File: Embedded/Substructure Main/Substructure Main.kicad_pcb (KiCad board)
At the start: 2 copper layers, 47 parts, among them J1 MicroSD, J2 C Pins, U1 G0 FFC, U2 G1 FFC, U3 S FFC, U4 USB2513B_Bi, U5 MCP7940N-xMNY, U6 INA220AIDGSR, U8 F FFC, Y1 24MHz 18pF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

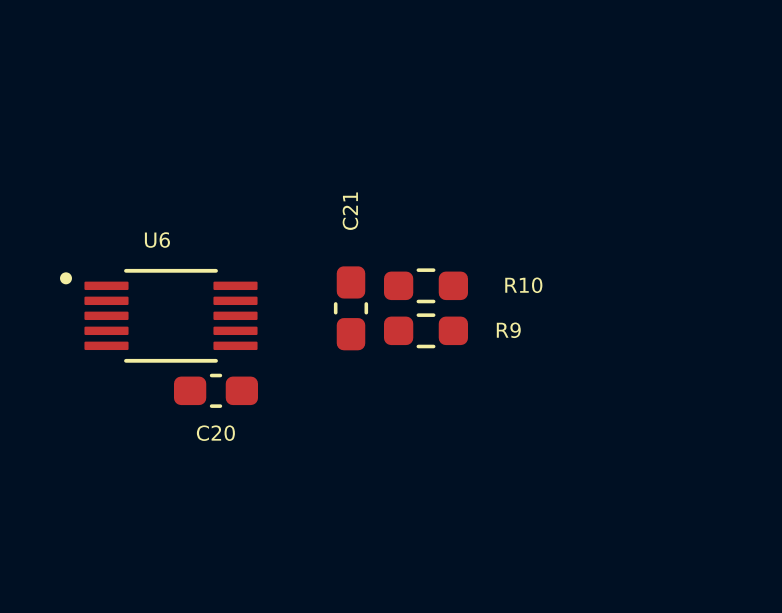
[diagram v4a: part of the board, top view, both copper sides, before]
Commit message: Added Shunt Resistor Footprint to PCB
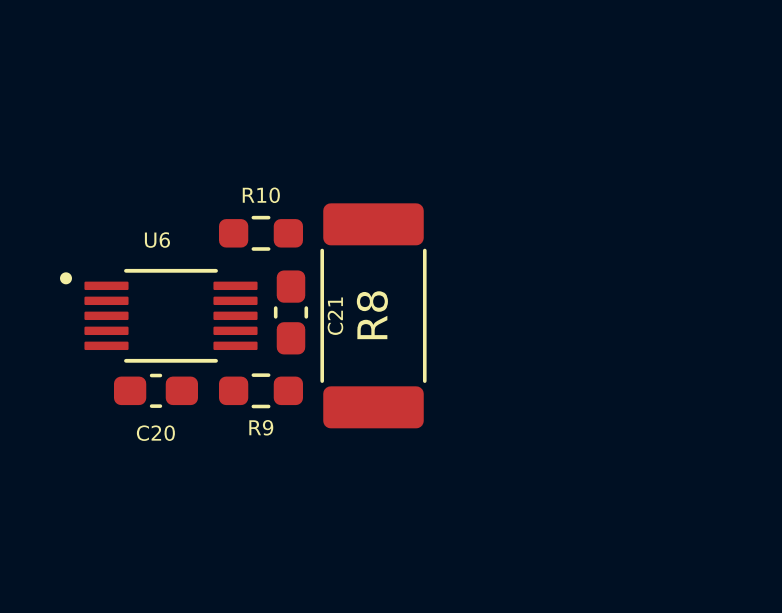
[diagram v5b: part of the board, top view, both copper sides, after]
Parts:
- added R8: Shunt, Resistor_SMD:R_2512_6332Metric_Pad1.40x3.35mm_HandSolder, F.Cu at (34.8, 184.5)
- moved R9 5.85 mm to (31.0, 187.0)
- moved R10 5.77 mm to (31.0, 181.8)
- moved C21 2.00 mm to (32.0, 184.4)
- moved C20 2.00 mm to (27.5, 187.0)
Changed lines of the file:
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@@
 	(footprint "Capacitor_SMD:C_0603_1608Metric_Pad1.08x0.95mm_HandSolder"
 		(layer "F.Cu")
-		(at 29.5 187 180)
+		(at 27.5 187 180)
 		(descr "Capacitor SMD 0603 (1608 Metric), square (rectangular) end terminal, IPC_7351 nominal with elongated pad for handsoldering. (Body size source: IPC-SM-782 page 76, https://www.pcb-3d.com/wordpress/wp-content/uploads/ipc-sm-782a_amendment_1_and_2.pdf), generated with kicad-footprint-generator")
 		(tags "capacitor handsolder")
@@
 	(footprint "Resistor_SMD:R_0603_1608Metric_Pad0.98x0.95mm_HandSolder"
 		(layer "F.Cu")
-		(at 36.5 183.5 180)
+		(at 31 181.75 180)
 		(descr "Resistor SMD 0603 (1608 Metric), square (rectangular) end terminal, IPC_7351 nominal with elongated pad for handsoldering. (Body size source: IPC-SM-782 page 72, https://www.pcb-3d.com/wordpress/wp-content/uploads/ipc-sm-782a_amendment_1_and_2.pdf), generated with kicad-footprint-generator")
 		(tags "resistor handsolder")
 		(property "Reference" "R10"
-			(at -3.25 0 0)
+			(at 0 1.25 0)
 			(layer "F.SilkS")
 			(effects
@@
 		)
 	)
+	(footprint "Resistor_SMD:R_2512_6332Metric_Pad1.40x3.35mm_HandSolder"
+		(layer "F.Cu")
+		(at 34.75 184.5 90)
+		(descr "Resistor SMD 2512 (6332 Metric), square (rectangular) end terminal, IPC_7351 nominal with elongated pad for handsoldering. (Body size source: IPC-SM-782 page 72, https://www.pcb-3d.com/wordpress/wp-content/uploads/ipc-sm-782a_amendment_1_and_2.pdf), generated with kicad-footprint-generator")
+		(tags "resistor handsolder")
+		(property "Reference" "R8"
+			(at 0 0 90)
+			(layer "F.SilkS")
+			(effects
+				(font
+					(size 1 1)
+					(thickness 0.15)
+				)
+			)
+		)
+		(property "Value" "Shunt"
+			(at 0 2.62 90)
+			(layer "F.Fab")
+			(hide yes)
+			(effects
+				(font
+					(size 1 1)
+					(thickness 0.15)
+				)
+			)
+		)
+		(property "Footprint" "Resistor_SMD:R_2512_6332Metric_Pad1.40x3.35mm_HandSolder"
+			(at 0 0 90)
+			(unlocked yes)
+			(layer "F.Fab")
+			(hide yes)
+			(effects
+				(font
+					(size 1.27 1.27)
+					(thickness 0.15)
+				)
+			)
+		)
+		(property "Datasheet" ""
+			(at 0 0 90)
+			(unlocked yes)
+			(layer "F.Fab")
+			(hide yes)
+			(effects
+				(font
+					(size 1.27 1.27)
+					(thickness 0.15)
+				)
+			)
+		)
+		(property "Description" "Resistor"
+			(at 0 0 90)
+			(unlocked yes)
+			(layer "F.Fab")
+			(hide yes)
+			(effects
+				(font
+					(size 1.27 1.27)
+					(thickness 0.15)
+				)
+			)
+		)
+		(property ki_fp_filters "R_*")
+		(sheetname "Root")
+		(sheetfile "Substructure Main.kicad_sch")
+		(attr smd)
+		(fp_line
+			(start -2.177064 -1.71)
+			(end 2.177064 -1.71)
+			(stroke
+				(width 0.12)
+				(type solid)
+			)
+			(layer "F.SilkS")
+		)
+		(fp_line
+			(start -2.177064 1.71)
+			(end 2.177064 1.71)
+			(stroke
+				(width 0.12)
+				(type solid)
+			)
+			(layer "F.SilkS")
+		)
+		(fp_line
+			(start 4 -1.92)
+			(end 4 1.92)
+			(stroke
+				(width 0.05)
+				(type solid)
+			)
+			(layer "F.CrtYd")
+		)
+		(fp_line
+			(start -4 -1.92)
+			(end 4 -1.92)
+			(stroke
+				(width 0.05)
+				(type solid)
+			)
+			(layer "F.CrtYd")
+		)
+		(fp_line
+			(start 4 1.92)
+			(end -4 1.92)
+			(stroke
+				(width 0.05)
+				(type solid)
+			)
+			(layer "F.CrtYd")
+		)
+		(fp_line
+			(start -4 1.92)
+			(end -4 -1.92)
+			(stroke
+				(width 0.05)
+				(type solid)
+			)
+			(layer "F.CrtYd")
+		)
+		(fp_line
+			(start 3.15 -1.6)
+			(end 3.15 1.6)
+			(stroke
+				(width 0.1)
+				(type solid)
+			)
+			(layer "F.Fab")
+		)
+		(fp_line
+			(start -3.15 -1.6)
+			(end 3.15 -1.6)
+			(stroke
+				(width 0.1)
+				(type solid)
+			)
+			(layer "F.Fab")
+		)
+		(fp_line
+			(start 3.15 1.6)
+			(end -3.15 1.6)
+			(stroke
+				(width 0.1)
+				(type solid)
+			)
+			(layer "F.Fab")
+		)
+		(fp_line
+			(start -3.15 1.6)
+			(end -3.15 -1.6)
+			(stroke
+				(width 0.1)
+				(type solid)
+			)
+			(layer "F.Fab")
+		)
+		(fp_text user "${REFERENCE}"
+			(at 0 0 90)
+			(layer "F.Fab")
+			(effects
+				(font
+					(size 1 1)
+					(thickness 0.15)
+				)
+			)
+		)
+		(pad "1" smd roundrect
+			(at -3.05 0 90)
+			(size 1.4 3.35)
+			(layers "F.Cu" "F.Paste" "F.Mask")
+			(roundrect_rratio 0.178571)
+			(net 13 "+5VP")
+			(pintype "passive")
+		)
+		(pad "2" smd roundrect
+			(at 3.05 0 90)
+			(size 1.4 3.35)
+			(layers "F.Cu" "F.Paste" "F.Mask")
+			(roundrect_rratio 0.178571)
+			(net 51 "+5V")
+			(pintype "passive")
+		)
+		(model "${KICAD8_3DMODEL_DIR}/Resistor_SMD.3dshapes/R_2512_6332Metric.wrl"
+			(offset
+				(xyz 0 0 0)
+			)
+			(scale
+				(xyz 1 1 1)
+			)
+			(rotate
+				(xyz 0 0 0)
+			)
+		)
+	)
 	(footprint "Capacitor_SMD:C_0402_1005Metric_Pad0.74x0.62mm_HandSolder"
 		(layer "F.Cu")
@@
 	(footprint "Capacitor_SMD:C_0603_1608Metric_Pad1.08x0.95mm_HandSolder"
 		(layer "F.Cu")
-		(at 34 184.25 90)
+		(at 32 184.3875 90)
 		(descr "Capacitor SMD 0603 (1608 Metric), square (rectangular) end terminal, IPC_7351 nominal with elongated pad for handsoldering. (Body size source: IPC-SM-782 page 76, https://www.pcb-3d.com/wordpress/wp-content/uploads/ipc-sm-782a_amendment_1_and_2.pdf), generated with kicad-footprint-generator")
 		(tags "capacitor handsolder")
 		(property "Reference" "C21"
-			(at 3.25 0 90)
+			(at -0.1125 1.5 90)
 			(layer "F.SilkS")
 			(effects
@@
 	(footprint "Resistor_SMD:R_0603_1608Metric_Pad0.98x0.95mm_HandSolder"
 		(layer "F.Cu")
-		(at 36.5 185 180)
+		(at 31 187 180)
 		(descr "Resistor SMD 0603 (1608 Metric), square (rectangular) end terminal, IPC_7351 nominal with elongated pad for handsoldering. (Body size source: IPC-SM-782 page 72, https://www.pcb-3d.com/wordpress/wp-content/uploads/ipc-sm-782a_amendment_1_and_2.pdf), generated with kicad-footprint-generator")
 		(tags "resistor handsolder")
 		(property "Reference" "R9"
-			(at -2.75 0 0)
+			(at 0 -1.25 0)
 			(layer "F.SilkS")
 			(effects

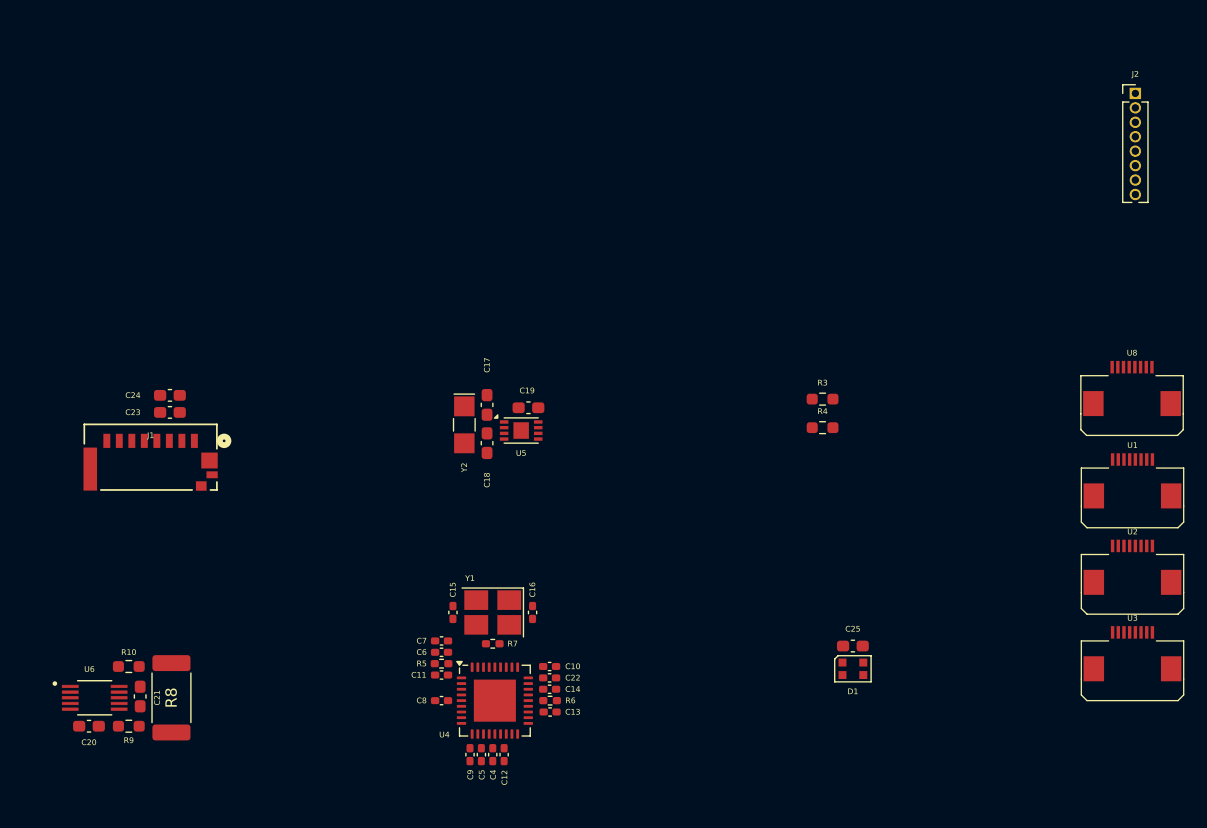
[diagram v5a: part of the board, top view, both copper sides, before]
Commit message: Added M Port FFC Footprint
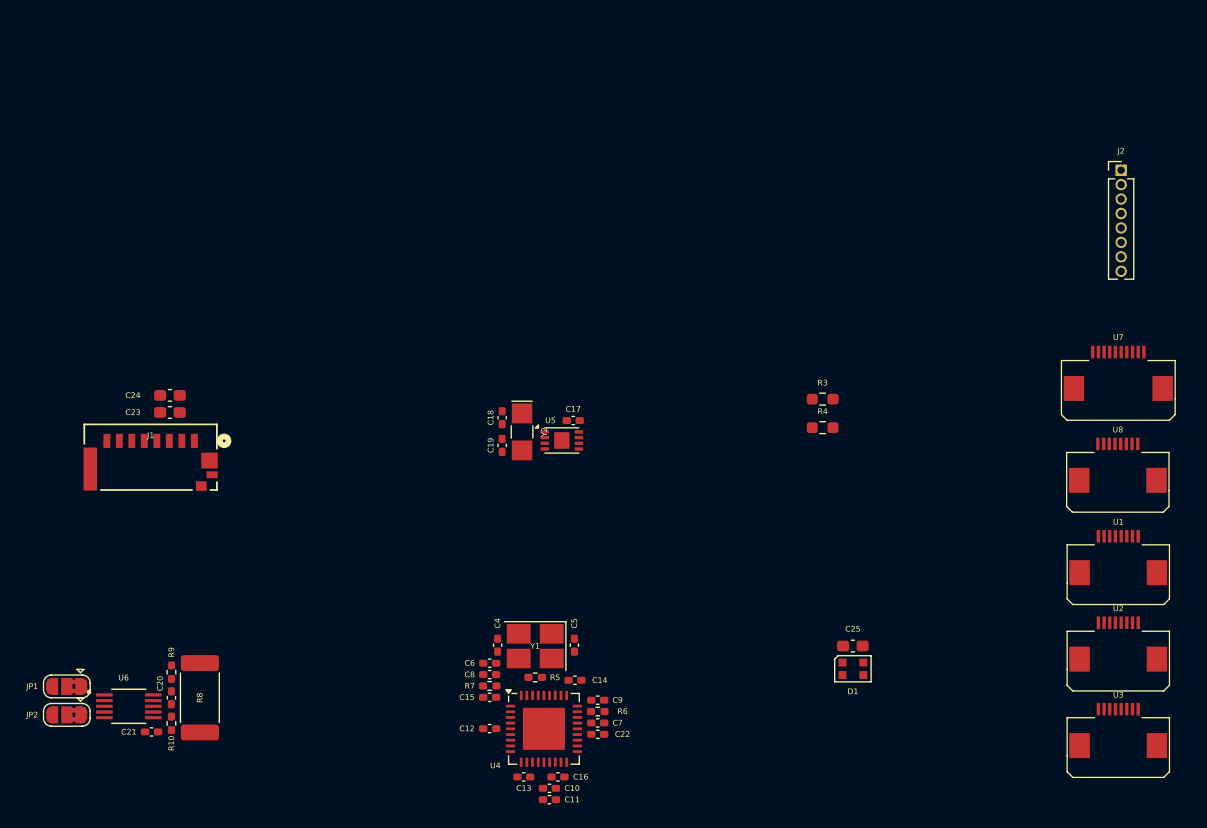
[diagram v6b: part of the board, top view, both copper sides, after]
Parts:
- added JP1: Bit Set, Jumper:SolderJumper-3_P1.3mm_Bridged2Bar12_RoundedPad1.0x1.5mm, F.Cu at (25.6, 183.5)
- added JP2: Bit Set, Jumper:SolderJumper-3_P1.3mm_Bridged2Bar12_RoundedPad1.0x1.5mm, F.Cu at (25.6, 186.0)
- added U7: M FFC, FFC:FFC-10-0.5, F.Cu at (118.0, 154.8)
- C10: value 0.1uF -> 1uF
- C15, C16: value 18pf -> 0.1uF
- C17: value 10pf -> 0.1uF; footprint Capacitor_SMD:C_0603_1608Metric_Pad1.08x0.95mm_HandSolder -> Capacitor_SMD:C_0402_1005Metric_Pad0.74x0.62mm_HandSolder
- C18: value 12pf -> 10pf; footprint Capacitor_SMD:C_0603_1608Metric_Pad1.08x0.95mm_HandSolder -> Capacitor_SMD:C_0402_1005Metric_Pad0.74x0.62mm_HandSolder
- C19: value 0.1uF -> 12pf; footprint Capacitor_SMD:C_0603_1608Metric_Pad1.08x0.95mm_HandSolder -> Capacitor_SMD:C_0402_1005Metric_Pad0.74x0.62mm_HandSolder
- C20: value 0.1uF -> 1uF; footprint Capacitor_SMD:C_0603_1608Metric_Pad1.08x0.95mm_HandSolder -> Capacitor_SMD:C_0402_1005Metric_Pad0.74x0.62mm_HandSolder
- C21: value 1uF -> 0.1uF; footprint Capacitor_SMD:C_0603_1608Metric_Pad1.08x0.95mm_HandSolder -> Capacitor_SMD:C_0402_1005Metric_Pad0.74x0.62mm_HandSolder
- C4: value 0.1uF -> 18pf
- C5: value 1uF -> 18pf
- R10, R9: footprint Resistor_SMD:R_0603_1608Metric_Pad0.98x0.95mm_HandSolder -> Resistor_SMD:R_0402_1005Metric_Pad0.72x0.64mm_HandSolder
- R5: value 12K -> 1M
- R7: value 1M -> 12K
- moved C7 15.5 mm to (72.2, 186.7), turned to 0 degrees
- moved C16 14.6 mm to (68.7, 191.5), turned to 0 degrees
- moved C11 14.5 mm to (68.0, 193.5), turned to 0 degrees
- moved C5 12.6 mm to (70.2, 179.9), turned to 90 degrees
- moved C9 12.2 mm to (72.2, 184.7), turned to 0 degrees
- moved C10 10.7 mm to (68.0, 192.5)
- moved C4 9.64 mm to (63.4, 179.9)
- moved R5 8.32 mm to (66.7, 182.7), turned to 180 degrees
- moved C15 8.13 mm to (62.7, 184.5), turned to 180 degrees
- moved C17 7.70 mm to (70.1, 160.1), turned to 180 degrees
- moved C20 7.67 mm to (34.8, 184.5), turned to -90 degrees
- moved J2 6.86 mm to (118.2, 138.1)
- moved U1 6.86 mm to (118.0, 170.9)
- moved U2 6.86 mm to (118.0, 178.6)
- moved U3 6.86 mm to (118.0, 186.2)
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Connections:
- C10 pad 1: +3V3 -> Net-(U4-CRFILT)
- C11 pad 1: +3V3 -> Net-(U4-CRFILT)
- C14 pad 1: Net-(U4-RESET_N) -> +3V3
- C15 pad 1: GND -> +3V3
- C15 pad 2: Net-(U4-XTALIN/CLKIN) -> GND
- C16 pad 1: GND -> +3V3
- C16 pad 2: Net-(U4-XTALOUT) -> GND
- C17 pad 1: Net-(U5-X1) -> +3V3
- C18 pad 1: Net-(U5-X2) -> Net-(U5-X1)
- C19 pad 1: +3V3 -> Net-(U5-X2)
- C20 pad 1: +3V3 -> Net-(U6-VBUS)
- C20 pad 2: GND -> Net-(U6-VIN-)
- C21 pad 1: Net-(U6-VBUS) -> +3V3
- C21 pad 2: Net-(U6-VIN-) -> GND
- C22 pad 1: +5VP -> +3V3
- C4 pad 1: Net-(U4-CRFILT) -> GND
- C4 pad 2: GND -> Net-(U4-XTALIN/CLKIN)
- C5 pad 1: Net-(U4-CRFILT) -> GND
- C5 pad 2: GND -> Net-(U4-XTALOUT)
- C7 pad 1: Net-(U4-PLLFILT) -> Net-(U4-RESET_N)
- C8 pad 1: +3V3 -> Net-(U4-PLLFILT)
- C9 pad 1: +3V3 -> +5VP
- R5 pad 1: GND -> Net-(U4-XTALOUT)
- R5 pad 2: Net-(U4-RBIAS) -> Net-(U4-XTALIN/CLKIN)
- R7 pad 1: Net-(U4-XTALOUT) -> GND
- R7 pad 2: Net-(U4-XTALIN/CLKIN) -> Net-(U4-RBIAS)
- U4 pad 3: HUD USB - -> HUD USB +
- U4 pad 4: HUD USB + -> Snoot USB -
- U4 pad 6: Snoot USB - -> Snoot USB +
- U4 pad 7: Snoot USB + -> HUD USB -
- U6 pad 3: (no net) -> unconnected-(U6-NC-Pad3)

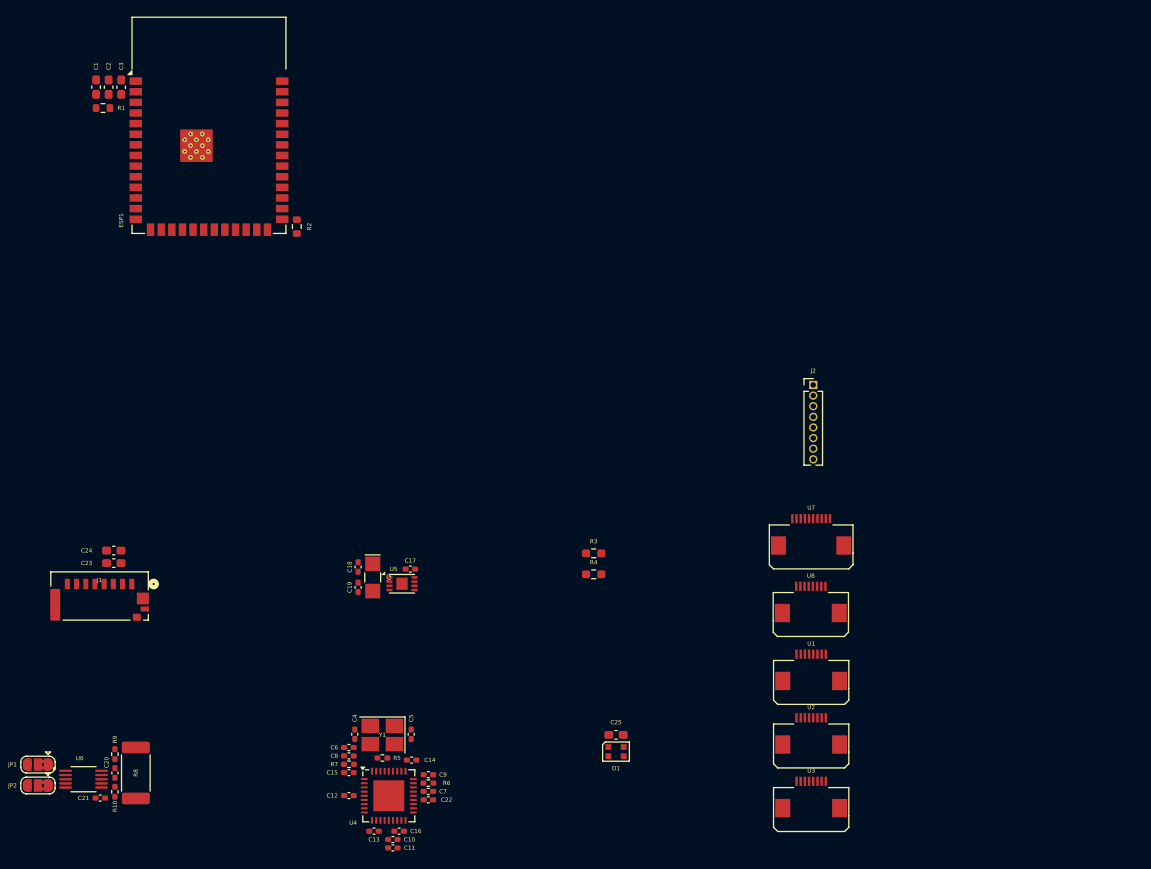
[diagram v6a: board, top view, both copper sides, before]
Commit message: Added Boot Switch Selection & Sensor Array
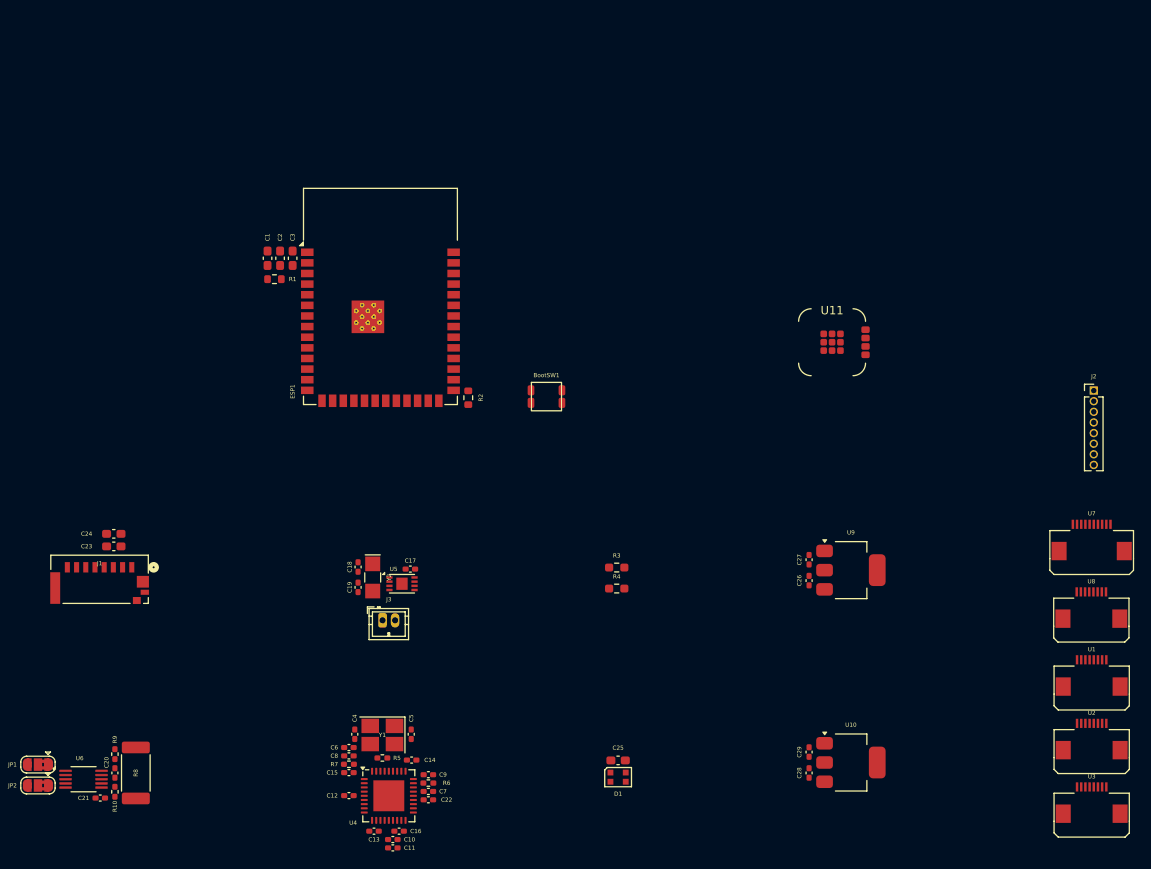
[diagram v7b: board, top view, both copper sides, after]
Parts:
- added BootSW1: SW_Push, Buttons:R-667843, F.Cu at (86.3, 139.5)
- added C26: 0.1uf, Capacitor_SMD:C_0402_1005Metric_Pad0.74x0.62mm_HandSolder, F.Cu at (117.8, 161.5)
- added C27: 10uf, Capacitor_SMD:C_0402_1005Metric_Pad0.74x0.62mm_HandSolder, F.Cu at (117.8, 159.0)
- added C28: 0.1uf, Capacitor_SMD:C_0402_1005Metric_Pad0.74x0.62mm_HandSolder, F.Cu at (117.8, 184.5)
- added C29: 10uf, Capacitor_SMD:C_0402_1005Metric_Pad0.74x0.62mm_HandSolder, F.Cu at (117.8, 182.0)
- added J3: Coin Cell, Connector_JST:JST_ZH_B2B-ZR_1x02_P1.50mm_Vertical, F.Cu at (66.8, 166.2)
- added U10: LD1117S50TR_SOT223, Package_TO_SOT_SMD:SOT-223-3_TabPin2, F.Cu at (122.8, 183.2)
- added U11: ~, Sensored:Sensored, F.Cu at (120.5, 133.0)
- added U9: LD1117S33TR_SOT223, Package_TO_SOT_SMD:SOT-223-3_TabPin2, F.Cu at (122.8, 160.2)
- R8: value Shunt -> Shunt CRF2512-FZ-R002ELF
- Y1: value 24MHz 18pF -> TSX-3225 24MF18X-C0
- Y2: value 32.768KHz 8pf -> CM7V-T1A
- moved U8 33.5 mm to (151.5, 163.5)
- moved J2 33.5 mm to (151.8, 138.8)
- moved U1 33.5 mm to (151.5, 171.6)
- moved U2 33.5 mm to (151.5, 179.2)
- moved U3 33.5 mm to (151.5, 186.8)
- moved U7 33.5 mm to (151.5, 155.4)
- moved C1 29.0 mm to (53.0, 123.0)
- moved C2 29.0 mm to (54.5, 123.0)
- moved C3 29.0 mm to (56.0, 123.0)
- moved ESP1 29.0 mm to (66.5, 127.5)
- moved R1 29.0 mm to (53.8, 125.5)
- moved R2 29.0 mm to (77.0, 139.6)
- moved R3 3.23 mm to (94.8, 159.9)
- moved R4 3.23 mm to (94.8, 162.4)
- moved C25 3.06 mm to (94.9, 183.0)
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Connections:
- R10 pad 1: +5V -> +5VP
- R8 pad 1: +5VP -> +5VS
- R8 pad 2: +5V -> +5VP
- R9 pad 1: +5VP -> +5VS
- U4 pad 3: HUD USB + -> HUD USB -
- U4 pad 4: Snoot USB - -> Snoot USB +
- U4 pad 6: Snoot USB + -> Snoot USB -
- U4 pad 7: HUD USB - -> HUD USB +
